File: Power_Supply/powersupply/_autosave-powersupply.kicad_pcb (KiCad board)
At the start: 2 copper layers, 60.8 x 63.3 mm, 70 parts, among them J1 Conn_01x03, J101 USB_B_Micro, J2 1x2, J3 1x2, Q1 Q_PMOS_GDS, SW1 KMR2, SW2 joystick-K1-1506DN-01, U1 B0505S-2WR2, U101 AZ1117E-3.3, U102 INA199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

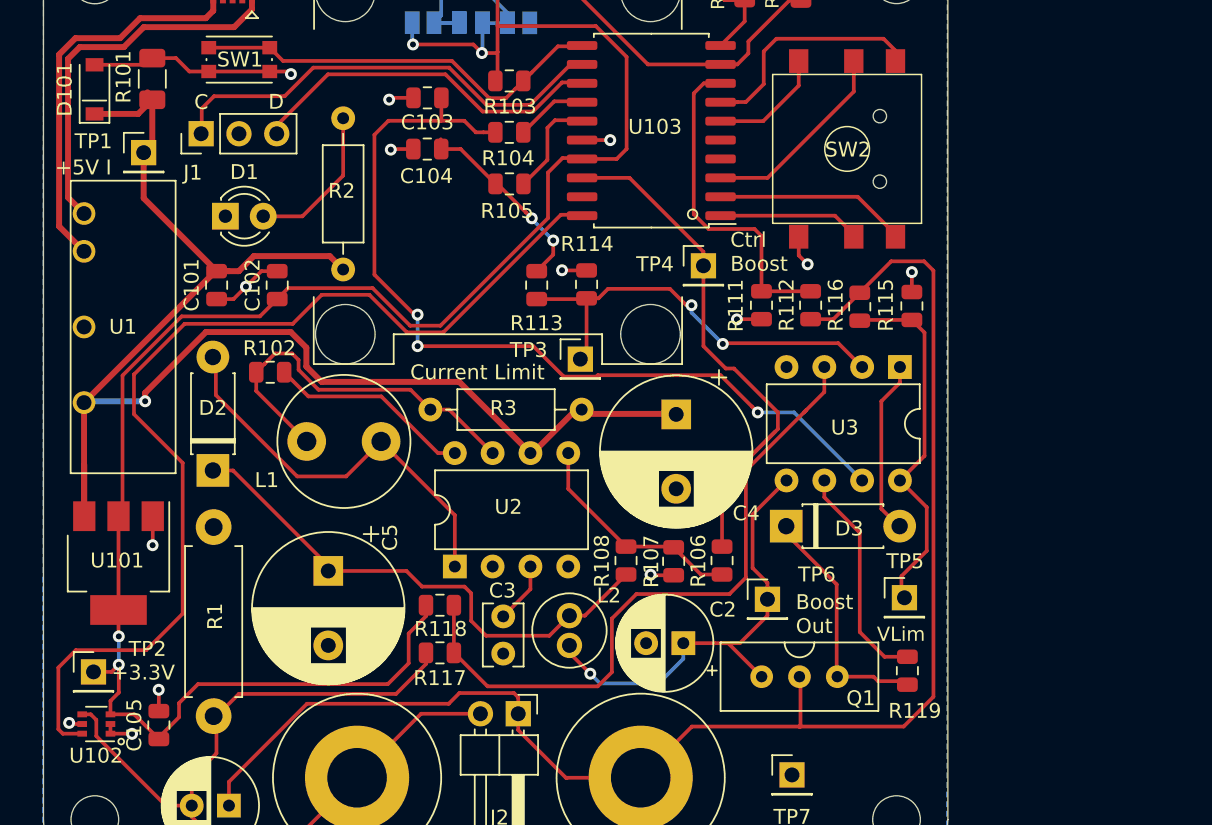
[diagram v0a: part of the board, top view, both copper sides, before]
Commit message: power supply layout updates
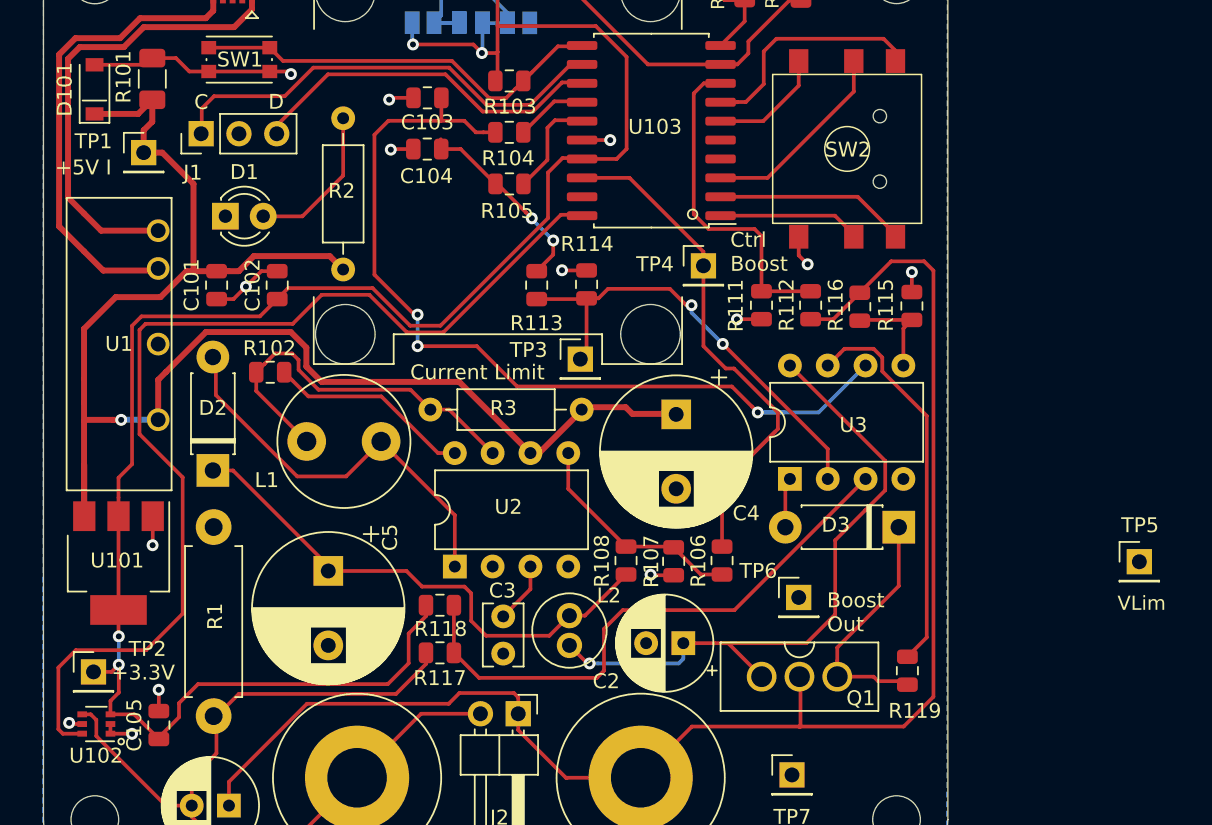
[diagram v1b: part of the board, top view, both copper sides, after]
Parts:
- removed G***: LOGO, powersupply:Logo
- moved TP5 16.0 mm to (102.4, 70.6)
- moved U3 10.5 mm to (79.0, 65.1), turned to 90 degrees
- moved D3 7.56 mm to (86.3, 68.3), turned to 180 degrees
- moved TP6 2.10 mm to (79.5, 73.0)
- moved U1 1.18 mm to (33.9, 56.0)
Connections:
- U3 pad 5: /Boost_out -> /Voltage_limit_divider
- U3 pad 6: Net-(R119-Pad2) -> /V_lin_ctrl
- U3 pad 7: /V_lin_ctrl -> Net-(R119-Pad2)
- U3 pad 8: /Voltage_limit_divider -> /Boost_out
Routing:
- net /Voltage_limit_divider: track 24.7 -> 6.82 mm
- net /Boost_out: track 31.2 -> 44.7 mm
- net Net-(R119-Pad2): track 15.1 -> 26.3 mm
- net Net-(D3-Pad2): track 12.1 -> 3.37 mm
- net Net-(R117-Pad1): track 45.7 -> 39.0 mm
- net /USB_GND: track 41.1 -> 46.7 mm
- net /USB_5V: track 25.8 -> 31.2 mm
- net +5V: track 99.3 -> 103.8 mm
- net /Current_limit_divider: track 28.7 -> 30.7 mm
- net +3V3: track 156.4 -> 158.1 mm
- net /V_lin_ctrl: track 59.5 -> 60.9 mm
- net /V_current_amplified: track 69.1 -> 70.3 mm
- net Net-(D3-Pad1): track 16.2 -> 16.8 mm
